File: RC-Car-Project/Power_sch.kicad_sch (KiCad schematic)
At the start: 30 parts, among them Q7 PMOS, U1 LMR16020PDDAR, U11 LMR16030PDDA

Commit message: I'm tired boss
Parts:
- added D8, D9: PMEG060V100EPD, Package_TO_SOT_SMD:Nexperia_CFP15_SOT-1289, symbol Diode:PMEG060V100EPD
- added TP1: TestPoint, Connector_PinHeader_2.54mm:PinHeader_1x02_P2.54mm_Vertical, symbol Connector:TestPoint
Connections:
- net VDD_BATT: now also D9.1 (A), D9.2 (A); no longer C4.1, C5.1, C6.1, U11.2 (VIN), U11.3 (EN)
- new net: C4.1, C5.1, C6.1, D8.3 (K), D9.3 (K), TP1.1, U11.2 (VIN), U11.3 (EN)
- new net VDD_USB: D8.1 (A), D8.2 (A)

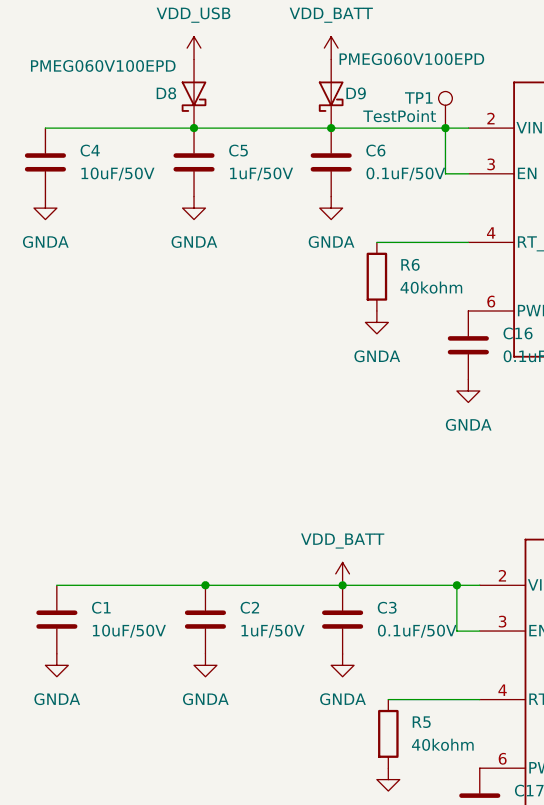
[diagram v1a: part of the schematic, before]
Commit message: change footprint of cap some part num added
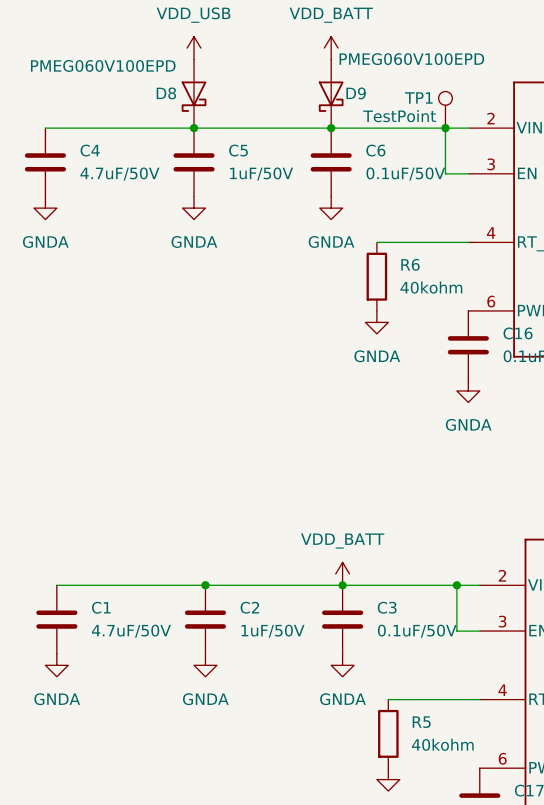
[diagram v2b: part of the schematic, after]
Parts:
- C1, C4: value 10uF/50V -> 4.7uF/50V; footprint Capacitor_SMD:C_0603_1608Metric -> Capacitor_SMD:C_1210_3225Metric; MANUF_PN (none) -> C1210X7S101-475KNE
- C2, C5: MANUF_PN (none) -> GRM188D72A105KE01D
- C3, C6: MANUF_PN (none) -> C0603X7R101-104KNP
- L1, L2: MANUF_PN (none) -> 74438357082
- Q7: MANUF_PN (none) -> SPP80P06PHXKSA1
- U1: MANUF_PN (none) -> LMR16020PDDAR
- U11: MANUF_PN (none) -> LMR16030PDDA

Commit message: add parts
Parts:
- C16, C17: value 0.1uF/50V -> 0.1uF/16V; MANUF_PN (none) -> C0603C104K4RACTU
- C7: MANUF_PN (none) -> C0603C104K4RACTU
- D3, D4: MANUF_PN (none) -> MBRS360T3G
- D8, D9: MANUF_PN (none) -> PMEG060V100EPDZ
- R5, R6: MANUF_PN (none) -> RT0603BRD0740KL
- R7: MANUF_PN (none) -> ERJ-3EKF3403V
- R8: MANUF_PN (none) -> RC0603FR-07100KL
- R9: MANUF_PN (none) -> RC0603FR-07150KL
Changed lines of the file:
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@@
 			)
 		)
-		(property "Value" "0.1uF/50V"
+		(property "Value" "0.1uF/16V"
 			(at 127 102.8699 0)
 			(effects
@@
 			)
 		)
-		(property "MANUF_PN" ""
+		(property "MANUF_PN" "C0603C104K4RACTU"
 			(at 123.19 101.6 0)
 			(effects
@@
 			)
 		)
-		(property "MANUF_PN" ""
+		(property "MANUF_PN" "RT0603BRD0740KL"
 			(at 113.03 93.98 0)
 			(effects
@@
 			)
 		)
-		(property "MANUF_PN" ""
+		(property "MANUF_PN" "ERJ-3EKF3403V"
 			(at 176.53 88.9 0)
 			(effects
@@
 			)
 		)
-		(property "MANUF_PN" ""
+		(property "MANUF_PN" "MBRS360T3G"
 			(at 162.56 92.71 0)
 			(effects
@@
 			)
 		)
-		(property "MANUF_PN" ""
+		(property "MANUF_PN" "MBRS360T3G"
 			(at 163.83 143.51 0)
 			(effects
@@
 			)
 		)
-		(property "MANUF_PN" ""
+		(property "MANUF_PN" "RC0603FR-07150KL"
 			(at 177.8 139.7 0)
 			(effects
@@
 			)
 		)
-		(property "MANUF_PN" ""
+		(property "MANUF_PN" "RT0603BRD0740KL"
 			(at 114.3 144.78 0)
 			(effects
@@
 			)
 		)
-		(property "MANUF_PN" ""
+		(property "MANUF_PN" "C0603C104K4RACTU"
 			(at 162.56 77.47 0)
 			(effects
@@
 			)
 		)
-		(property "Value" "0.1uF/50V"
+		(property "Value" "0.1uF/16V"
 			(at 128.27 153.6699 0)
 			(effects
@@
 			)
 		)
-		(property "MANUF_PN" ""
+		(property "MANUF_PN" "C0603C104K4RACTU"
 			(at 124.46 152.4 0)
 			(effects
@@
 			)
 		)
-		(property "MANUF_PN" ""
+		(property "MANUF_PN" "PMEG060V100EPDZ"
 			(at 107.95 73.66 0)
 			(effects
@@
 			)
 		)
-		(property "MANUF_PN" ""
+		(property "MANUF_PN" "RC0603FR-07100KL"
 			(at 176.53 99.06 0)
 			(effects
@@
 			)
 		)
-		(property "MANUF_PN" ""
+		(property "MANUF_PN" "PMEG060V100EPDZ"
 			(at 92.71 73.66 0)
 			(effects

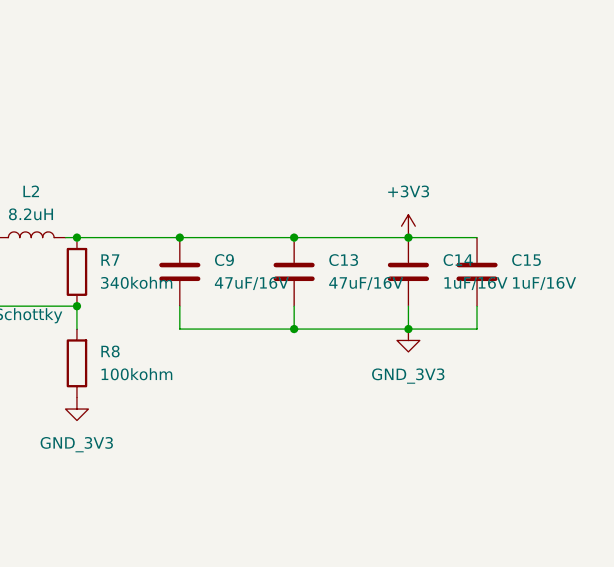
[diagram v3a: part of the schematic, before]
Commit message: change cap ratings
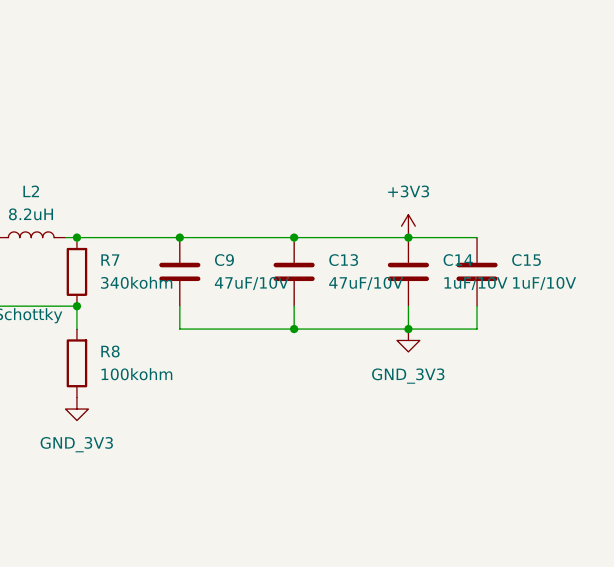
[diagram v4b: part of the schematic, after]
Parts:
- C13, C9: value 47uF/16V -> 47uF/10V
- C14, C15: value 1uF/16V -> 1uF/10V
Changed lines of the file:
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@@
 			)
 		)
-		(property "Value" "47uF/16V"
+		(property "Value" "47uF/10V"
 			(at 204.47 90.1699 0)
 			(effects
@@
 			)
 		)
-		(property "Value" "1uF/16V"
+		(property "Value" "1uF/10V"
 			(at 217.17 90.1699 0)
 			(effects
@@
 			)
 		)
-		(property "Value" "47uF/16V"
+		(property "Value" "47uF/10V"
 			(at 191.77 90.1699 0)
 			(effects
@@
 			)
 		)
-		(property "Value" "1uF/16V"
+		(property "Value" "1uF/10V"
 			(at 224.79 90.1699 0)
 			(effects

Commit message: Resistor manuf PNs labelled
resistor manufacturer part numbers added
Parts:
- R10: MANUF_PN (none) -> RC0603FR-0710KL
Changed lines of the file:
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@@
 			)
 		)
-		(property "MANUF_PN" ""
+		(property "MANUF_PN" "RC0603FR-0710KL"
 			(at 177.8 149.86 0)
 			(effects
